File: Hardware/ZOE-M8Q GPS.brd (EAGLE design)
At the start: 25.4 x 25.4 mm, 23 parts, among them J4 U.FL, U1 UBLOX_ZOE_M8-0-10, Y1 32.768kHz

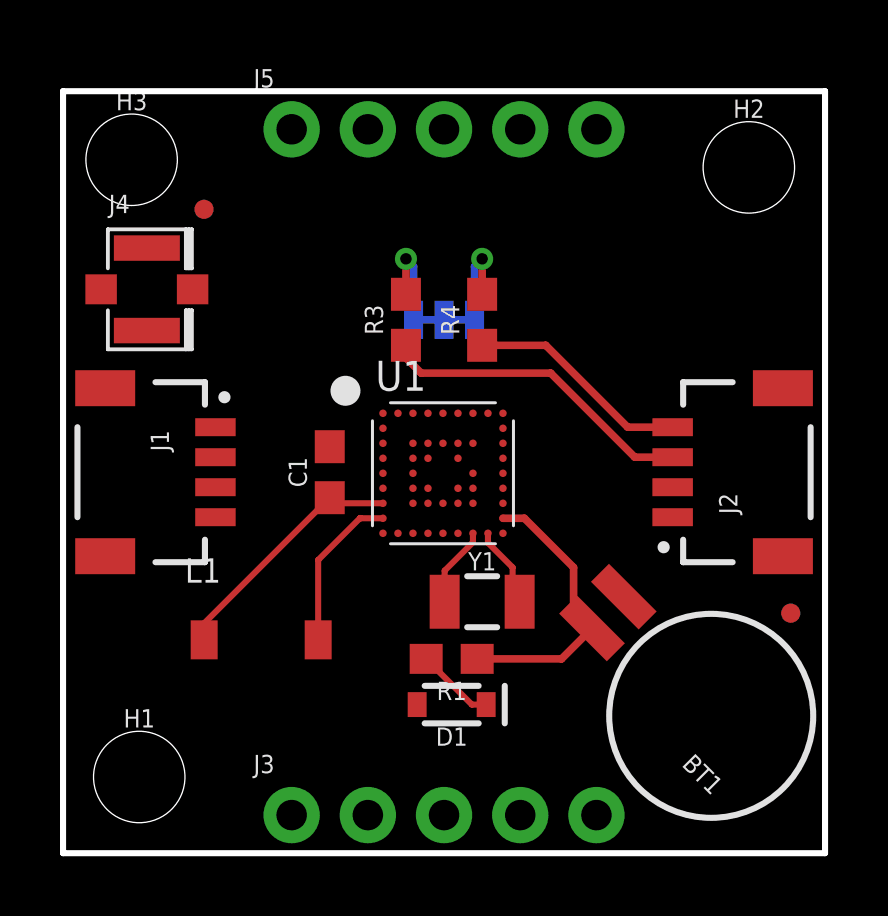
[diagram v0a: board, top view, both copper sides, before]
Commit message: Adds Buzzard Labels, finishes tracework (see description)
* Moves diode and reistor
* Fixes TSTOP on LGA
* Moves uFL connector
* Moves Jumpers
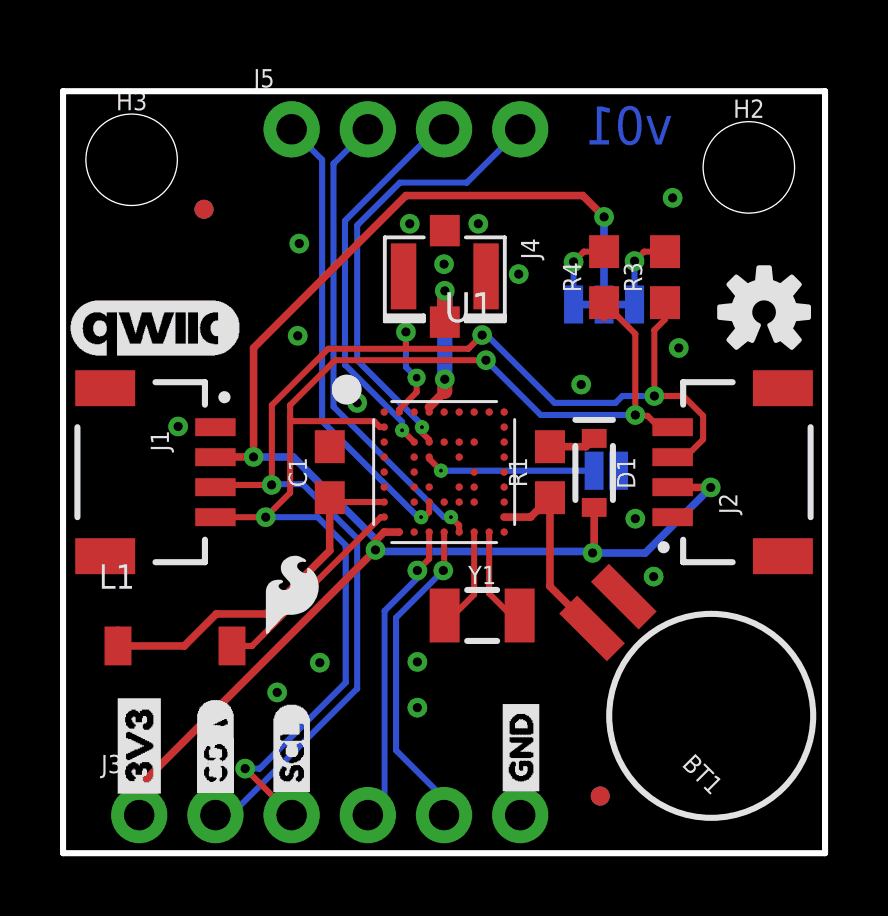
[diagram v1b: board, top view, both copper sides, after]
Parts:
- removed H1: STAND-OFFTIGHT, SparkFun-Hardware:STAND-OFF-TIGHT
- added JP1: JUMPER-SMT_2_NO_SILK, SparkFun-Jumpers:SMT-JUMPER_2_NO_SILK
- added LOGO1: SFE_LOGO_NAME.1_INCH, SparkFun-Aesthetics:SFE_LOGO_NAME_.1
- added LOGO2: OSHW-LOGOS, SparkFun-Aesthetics:OSHW-LOGO-S
- added LOGO3: SFE_LOGO_FLAME.1_INCH, SparkFun-Aesthetics:SFE_LOGO_FLAME_.1
- added U$1, U$10: (no value), Labels:3V3-03
- added U$11: (no value), INT:INT0
- added U$12: (no value), RESET:RESET0
- added U$13: (no value), TIMEPULSE:TIMEPULSE0
- added U$14: (no value), SAFEBOOT:SAFEBOOT0
- added U$15, U$19: (no value), Labels:QWIIC_COPYRIGHT_SMALL
- added U$16: (no value), ZOE-M8Q:ZOE#M8Q0
- added U$17: (no value), SPI_JUMPER:SPI0
- added U$18: (no value), I2C_PU:I2C_PU0
- added U$2: (no value), SDA:SDA0
- added U$3: (no value), SCL:SCL0
- added U$4, U$7: (no value), GND:GND0
- added U$5: (no value), RX_MOSI:RXI#MOSI0
- added U$6: (no value), TXO_MISO:TXO#MISO0
- added U$8: (no value), CLK:CLK0
- added U$9: (no value), CS:CS0
- J3: device SparkFun-Connectors:1X05_NO_SILK -> SparkFun-Connectors:1X06_NO_SILK
- J5: device SparkFun-Connectors:1X05_NO_SILK -> SparkFun-Connectors:1X04_NO_SILK
- moved J4 9.94 mm to (12.7, 19.2), turned to 270 degrees
- moved D1 9.07 mm to (17.7, 12.7), turned to 270 degrees
- moved FD2 8.80 mm to (17.9, 1.91)
- moved FD4 8.80 mm to (17.9, 1.91)
- moved R3 8.75 mm to (20.1, 19.2)
- moved R1 7.03 mm to (16.2, 12.7), turned to 90 degrees
- moved JP2 5.36 mm to (18.0, 18.3)
- moved J3 5.08 mm to (2.54, 1.27)
- moved R4 4.31 mm to (18.0, 19.2)
- moved U1 3.23 mm to (12.7, 12.7)
- moved L1 2.88 mm to (3.73, 6.91)
- moved Y1 0.46 mm to (14.0, 7.92)
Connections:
- removed net LNA_EN: U1.35
- removed net N$16: U1.36
- removed net N$4: JP2.1, R4.2
- removed net N$9: U1.50
- removed net RXD/MOSI: U1.22
- removed net TXD/MISO: U1.21
- new net N$1: JP2.1, R3.2
- new net RXI/MOSI: J3.4, U1.22
- new net TXO/MISO: J3.5, U1.21
- net 3.3V: now also J3.1
- net D_SEL: now also JP1.1
- net GND: now also J3.6, JP1.2
- net INT: now also J5.1
- net N$3: now also R4.2; no longer R3.2
- net RESET: now also J5.2
- net SAFEBOOT: now also J5.4
- net SCL/CLK: now also J3.3
- net SDA/CS: now also J3.2
- net TIMEPULSE: now also J5.3
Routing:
- net 3.3V: track 0.00 -> 55.7 mm, vias 0 -> 5
- net SCL/CLK: track 7.48 -> 42.5 mm, vias 0 -> 4
- net SDA/CS: track 10.7 -> 45.3 mm, vias 0 -> 5
- net RESET: track 0.00 -> 15.8 mm, vias 0 -> 1
- net INT: track 0.00 -> 15.4 mm, vias 0 -> 1
- net SAFEBOOT: track 0.00 -> 15.0 mm, vias 0 -> 1
- net TIMEPULSE: track 0.00 -> 12.9 mm, vias 0 -> 1
- net TXO/MISO: track 0.00 -> 10.8 mm, vias 0 -> 1
- net RXI/MOSI: track 0.00 -> 10.3 mm, vias 0 -> 1
- net D_SEL: track 0.00 -> 5.72 mm, vias 0 -> 1
- net N$5: track 0.00 -> 5.30 mm, vias 0 -> 2
- net N$6: track 8.32 -> 12.7 mm
- net N$4: track 3.32 -> 0.00 mm, vias 1 -> 0
- net V_BATT: track 9.57 -> 6.73 mm
- net N$1: track 0.00 -> 2.59 mm, vias 0 -> 1
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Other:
- board text added: "v01"

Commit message: Updates silk, adds new inductor, adds LED
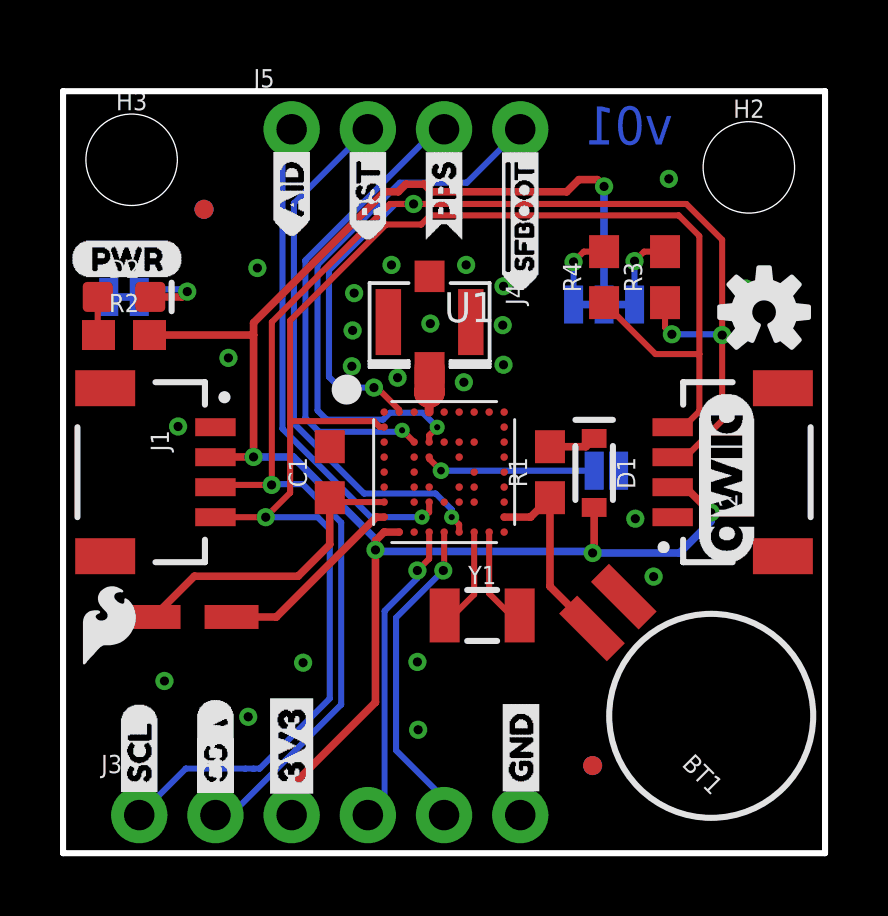
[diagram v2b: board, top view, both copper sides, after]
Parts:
- removed L1: 2.2µH/±20%/1.5A, SparkFun-Coils:INDUCTOR_2.2UH
- added D2: RED, SparkFun-LED:LED-0603
- added JP4: JUMPER-SMT_2_NC_TRACE_SILK, SparkFun-Jumpers:SMT-JUMPER_2_NC_TRACE_SILK
- added R2: 1k, SparkFun-Resistors:0603
- added U$20: 2.2UH_SHIELDED_INDUCTOR, temp:0806
- added U$21: (no value), AID:AID0
- added U$22: (no value), RESET:RST0
- added U$23: (no value), TIMEPULSE:PPS0
- added U$24: (no value), SAFEBOOT:#SFBOOT0
- added U$25: (no value), LED:LED0
- added U$26: (no value), Labels:PWR-()-03
- U$11: device INT:INT0 -> AID:AID0
- U$12: device RESET:RESET0 -> RESET:RST0
- U$13: device TIMEPULSE:TIMEPULSE0 -> TIMEPULSE:PPS0
- U$14: device SAFEBOOT:SAFEBOOT0 -> SAFEBOOT:#SFBOOT0
- moved U$15 19.7 mm to (22.1, 12.5), turned to 90 degrees
- moved LOGO3 6.18 mm to (1.52, 7.62)
- moved U$1 5.08 mm to (7.62, 1.52)
- moved U$10 5.08 mm to (7.62, 1.52)
- moved U$3 5.08 mm to (2.54, 1.68)
- moved U$8 5.08 mm to (2.54, 1.68)
- moved U$13 4.11 mm to (12.7, 20.4)
- moved U$14 2.11 mm to (15.2, 18.6), flipped to the top
- moved J4 1.61 mm to (12.2, 17.7)
- moved U$12 1.45 mm to (10.2, 20.4)
- moved FD2 1.05 mm to (17.7, 2.92)
- moved FD4 1.05 mm to (17.7, 2.92)
- moved U$11 0.05 mm to (7.62, 20.5)
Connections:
- new net N$4: D2.A, R2.1
- new net N$8: D2.C, JP4.2
- net 3.3V: now also J3.3, R2.2; no longer J3.1
- net GND: now also JP4.1
- net N$6: now also U$20.P$1; no longer L1.P$1
- net N$7: now also U$20.P$2; no longer L1.P$2
- net SCL/CLK: now also J3.1; no longer J3.3
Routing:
- net SDA/CS: track 45.3 -> 60.3 mm
- net SCL/CLK: track 42.5 -> 53.9 mm, vias 4 -> 1
- net N$5: track 5.30 -> 1.48 mm, vias 2 -> 0
- net SAFEBOOT: track 15.0 -> 18.5 mm
- net 3.3V: track 55.7 -> 59.0 mm
- net N$8: track 0.00 -> 3.04 mm, vias 0 -> 1
- net TIMEPULSE: track 12.9 -> 15.7 mm
- net RESET: track 15.8 -> 18.1 mm
- net N$6: track 12.7 -> 10.3 mm
- net N$4: track 0.00 -> 1.28 mm
- net INT: track 15.4 -> 16.6 mm
- net N$15: track 3.88 -> 3.35 mm

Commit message: Adds pinout for FTDI connection, updates NDUC and ZOE footprints with tkeepout and tdocu, fixes silk labels
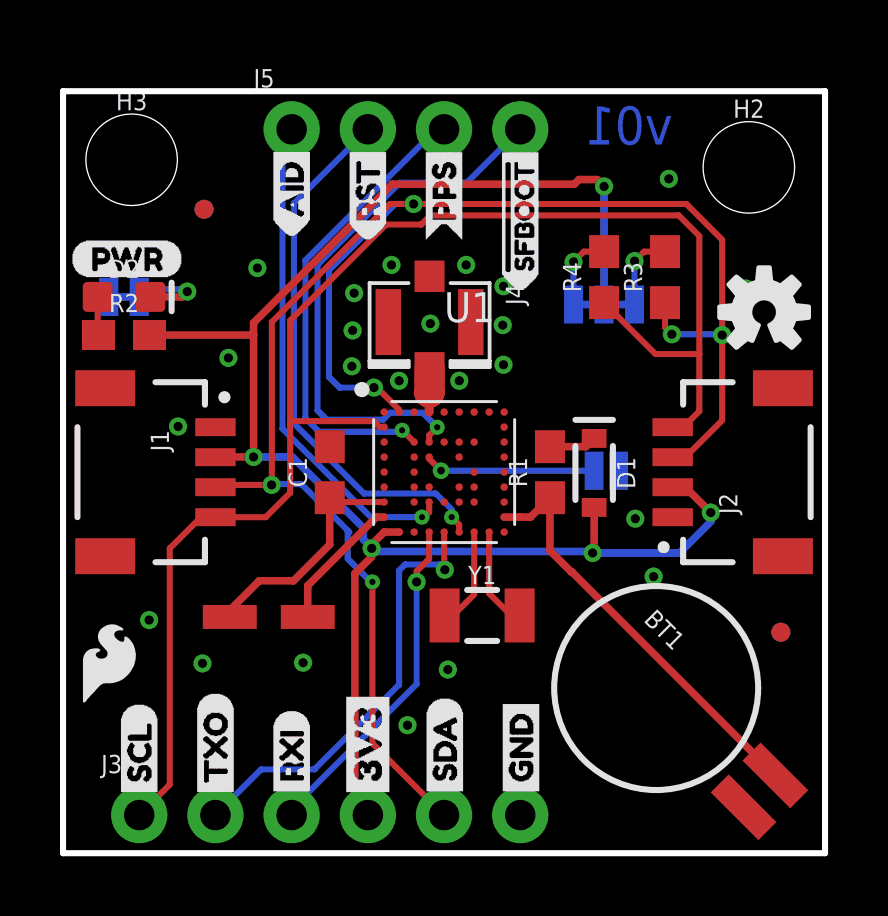
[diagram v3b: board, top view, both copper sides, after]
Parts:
- removed U$9: (no value), CS:CS0
- added U$27: (no value), MOSI:MOSI0
- U$15: device Labels:QWIIC_COPYRIGHT_SMALL -> TX:TXO0
- U$19: device Labels:QWIIC_COPYRIGHT_SMALL -> RX:RXI0
- U$20: device temp:0806 -> temp:0806_NDUC
- U$5: device RX_MOSI:RXI#MOSI0 -> CS:CS0
- U$6: device TXO_MISO:TXO#MISO0 -> MISO:MISO0
- moved U$15 20.2 mm to (5.08, 1.65)
- moved U$19 16.1 mm to (7.62, 1.70), flipped to the top, turned to 90 degrees
- moved FD2 7.69 mm to (23.9, 7.37)
- moved FD4 7.69 mm to (23.9, 7.37)
- moved U$2 7.65 mm to (12.7, 1.70)
- moved U$6 7.62 mm to (5.08, 1.65)
- moved U$5 2.57 mm to (12.7, 1.68)
- moved U$1 2.54 mm to (10.2, 1.57)
- moved U$10 2.54 mm to (10.2, 1.57)
- moved U$20 2.54 mm to (6.86, 7.87)
- moved BT1 2.06 mm to (19.8, 5.51), turned to 315 degrees
- moved LOGO3 1.27 mm to (1.52, 6.35)
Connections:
- net 3.3V: now also J3.4; no longer J3.3
- net RXI/MOSI: now also J3.3; no longer J3.4
- net SDA/CS: now also J3.5; no longer J3.2
- net TXO/MISO: now also J3.2; no longer J3.5
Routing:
- net V_BATT: track 6.73 -> 14.2 mm
- net SCL/CLK: track 53.9 -> 49.3 mm, vias 1 -> 0
- net TXO/MISO: track 10.8 -> 14.7 mm
- net N$6: track 10.3 -> 7.93 mm
- net N$7: track 6.47 -> 4.54 mm
- net RXI/MOSI: track 10.3 -> 11.3 mm
- net 3.3V: track 59.0 -> 58.1 mm
- net SDA/CS: track 60.3 -> 59.8 mm, vias 5 -> 6

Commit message: Adds more silk labels, adds tkeepout around oscillator and more ground vias
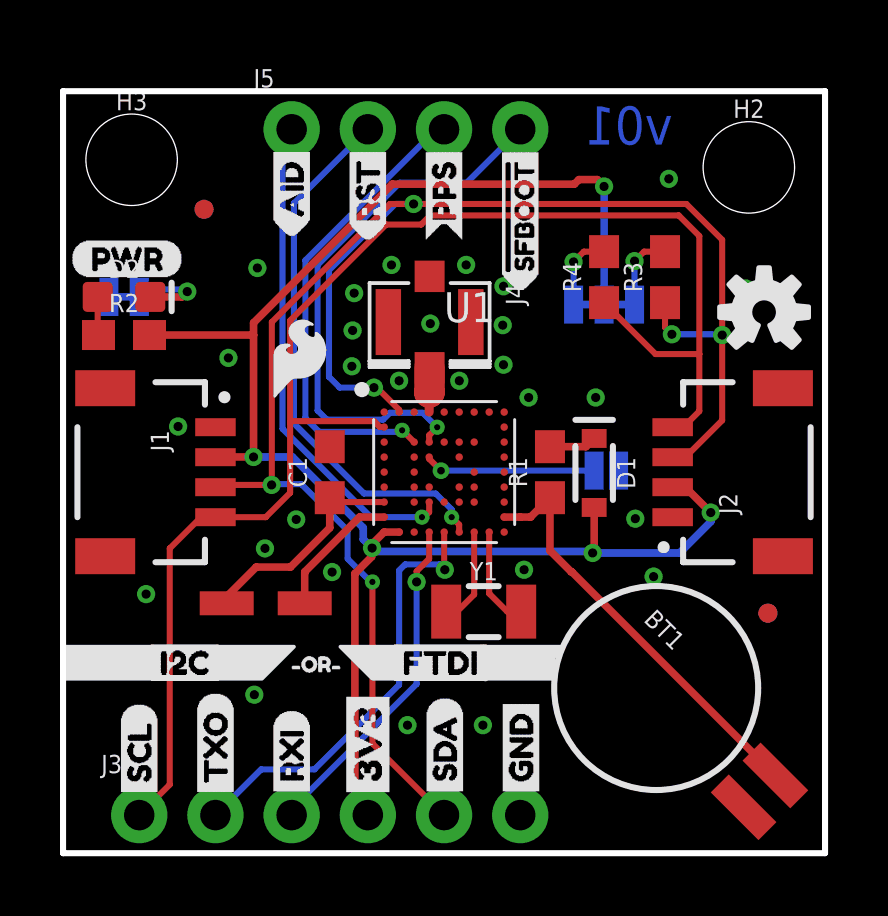
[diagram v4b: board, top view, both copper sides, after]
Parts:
- added U$28: (no value), I2C_MINOR:I2C0
- added U$29: (no value), FTDI_SMALL:FTDI0
- added U$30: (no value), OR:#OR#0
- added U$9: (no value), SPI_MAJOR:SPI0
- moved LOGO3 12.0 mm to (7.87, 16.5)
- moved FD2 0.77 mm to (23.5, 8.00)
- moved FD4 0.77 mm to (23.5, 8.00)
- moved U$20 0.47 mm to (6.76, 8.33)
- moved Y1 0.14 mm to (14.0, 8.05)
- moved U$18 0.13 mm to (20.4, 16.5)
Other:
- board text added: "Units in Inches"

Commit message: Removes one qwiic connector to make space for super capacitor, adds active antenna components (see description)
* Adds 10 ohm resistor, ferrite bead, and 47pF capacitor.
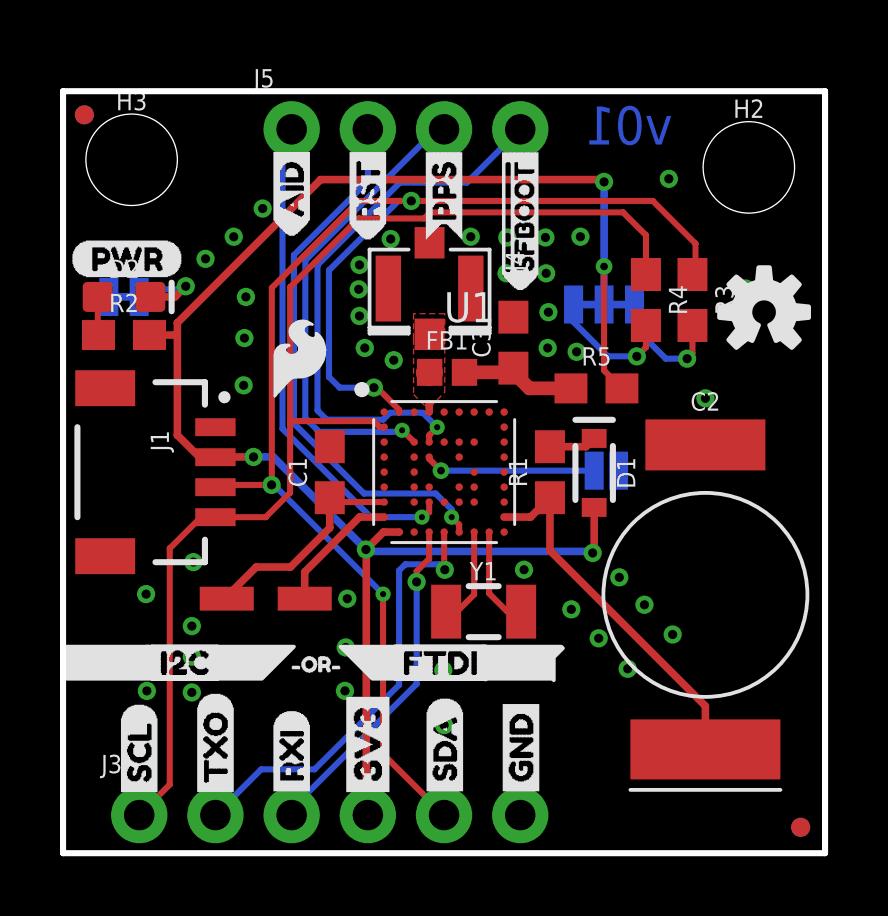
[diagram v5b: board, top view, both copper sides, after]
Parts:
- removed BT1: 6.8MM_COIN_CELL, SparkFun-Batteries:BATTCON-6.8MM
- removed J2: (no value), SparkFun-Connectors:JST04_1MM_RA
- removed U$20: 2.2UH_SHIELDED_INDUCTOR, temp:0806_NDUC
- added C2: .22F-SUPERCAP, SparkFun-Capacitors:DSK-RADIAL-4.8MM
- added C3: 47pF, SparkFun-Capacitors:0603
- added FB1: FERRITE_BEAD-120_OHM-0402, SparkFun-Coils:0402
- added L1: 2.2UH_SHIELDED_INDUCTOR, temp:0806_NDUC
- added R5: 10, SparkFun-Resistors:0603
- LOGO1: value SFE_LOGO_NAME.1_INCH -> SFE_LOGO_NAME_FLAME.1_INCH; device SparkFun-Aesthetics:SFE_LOGO_NAME_.1 -> SparkFun-Aesthetics:SFE_LOGO_NAME_FLAME_.1
- moved FD2 7.22 mm to (24.6, 0.86)
- moved FD4 7.22 mm to (24.6, 0.86)
- moved FD1 5.08 mm to (0.71, 24.6)
- moved FD3 5.08 mm to (0.71, 24.6)
- moved LOGO1 3.81 mm to (9.65, 15.0)
- moved R4 1.59 mm to (19.4, 18.4), turned to 270 degrees
- moved R3 1.19 mm to (21.0, 18.4), turned to 270 degrees
- moved J4 1.12 mm to (12.2, 18.8)
- moved U$16 0.53 mm to (12.8, 12.6)
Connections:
- removed net N$5: J4.FEED, U1.4
- new net ANT: FB1.1, J4.FEED, U1.4
- new net N$9: C3.1, FB1.2, R5.1
- net 3.3V: now also R5.2; no longer J2.2
- net GND: now also C2.-, C3.2; no longer BT1.-, J2.1
- net N$6: now also L1.P$1; no longer U$20.P$1
- net N$7: now also L1.P$2; no longer U$20.P$2
- net SCL/CLK: no longer J2.4
- net SDA/CS: no longer J2.3
- net V_BATT: now also C2.+; no longer BT1.+
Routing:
- net SDA/CS: track 59.7 -> 49.0 mm, vias 6 -> 4
- net SCL/CLK: track 49.3 -> 38.7 mm
- net N$9: track 0.00 -> 3.91 mm
- net V_BATT: track 14.2 -> 12.3 mm
- net N$3: track 2.58 -> 4.32 mm
- net N$1: track 2.59 -> 4.27 mm
- net 3.3V: track 58.1 -> 56.5 mm
- net N$5: track 1.48 -> 0.00 mm
- added copper zone on layer 1, net ANT

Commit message: Adds more ground stitching vias
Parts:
- moved LOGO3 3.10 mm to (4.90, 17.4)
- moved LOGO2 0.82 mm to (23.4, 17.2)
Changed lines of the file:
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@@
 <text x="20.32" y="23.622" size="1.27" layer="16" font="vector" ratio="15" rot="MR0">v01</text>
 <polygon width="0.127" layer="21">
-<vertex x="5.1308" y="5.8166"/>
-<vertex x="6.6294" y="5.8166"/>
-<vertex x="7.6962" y="6.8834"/>
-<vertex x="5.1054" y="6.8834"/>
-<vertex x="5.1054" y="5.8166"/>
+<vertex x="5.1308" y="5.801359375"/>
+<vertex x="6.614159375" y="5.801359375"/>
+<vertex x="7.711440625" y="6.898640625"/>
+<vertex x="5.1181" y="6.898640625"/>
+<vertex x="5.1181" y="5.8166"/>
 <vertex x="5.1562" y="5.8166"/>
 <vertex x="5.1562" y="5.842"/>
@@
 </polygon>
 <polygon width="0.127" layer="21">
-<vertex x="11.303" y="5.8166"/>
-<vertex x="10.3124" y="5.8166"/>
-<vertex x="9.2456" y="6.8834"/>
-<vertex x="11.15229375" y="6.8834"/>
-</polygon>
-<polygon width="0.127" layer="21">
-<vertex x="3.0226" y="6.8834"/>
-<vertex x="0" y="6.8834"/>
-<vertex x="0" y="5.8166"/>
-<vertex x="3.0734" y="5.8166"/>
+<vertex x="11.300459375" y="5.8013625"/>
+<vertex x="10.3276375" y="5.8013625"/>
+<vertex x="9.2329" y="6.8961"/>
+<vertex x="11.162453125" y="6.8961"/>
+</polygon>
+<polygon width="0.127" layer="21">
+<vertex x="3.0226" y="6.8961"/>
+<vertex x="0" y="6.8961"/>
+<vertex x="0" y="5.801359375"/>
+<vertex x="3.088640625" y="5.801359375"/>
 <vertex x="3.0226" y="5.8674"/>
 </polygon>
@@
 </polygon>
 <polygon width="0.127" layer="21">
-<vertex x="14.1732" y="5.8166"/>
-<vertex x="16.3068" y="5.8166"/>
-<vertex x="16.3576" y="5.7658"/>
-<vertex x="16.3576" y="6.5278"/>
-<vertex x="16.6624" y="6.8326"/>
-<vertex x="16.6116" y="6.8834"/>
-<vertex x="13.9192" y="6.8834"/>
-<vertex x="13.9192" y="5.9436"/>
-<vertex x="14.0716" y="5.7912"/>
-<vertex x="14.1732" y="5.8166"/>
+<vertex x="14.048459375" y="5.801359375"/>
+<vertex x="16.3449" y="5.801359375"/>
+<vertex x="16.3449" y="6.8707"/>
+<vertex x="16.3195" y="6.8961"/>
+<vertex x="13.9192" y="6.8961"/>
+<vertex x="13.9192" y="5.93061875"/>
 </polygon>
 <dimension x1="25.4" y1="25.4" x2="25.4" y2="0" x3="31.75" y3="12.7" textsize="1.27" textratio="15" layer="47" dtype="vertical" unit="inch"/>
@@
 <element name="U$10" library="Labels" package="3V3-03" value="" x="10.16" y="1.5748" smashed="yes" rot="MR90"/>
 <element name="LOGO1" library="SparkFun-Aesthetics" package="SFE_LOGO_NAME_FLAME_.1" value="SFE_LOGO_NAME_FLAME.1_INCH" x="9.652" y="14.986" smashed="yes" rot="MR0"/>
-<element name="LOGO2" library="SparkFun-Aesthetics" package="OSHW-LOGO-S" value="OSHW-LOGOS" x="23.368" y="18.034" smashed="yes"/>
+<element name="LOGO2" library="SparkFun-Aesthetics" package="OSHW-LOGO-S" value="OSHW-LOGOS" x="23.362921875" y="17.213578125" smashed="yes"/>
 <element name="U$16" library="ZOE-M8Q" package="ZOE#M8Q0" value="" x="12.7508" y="12.6238" smashed="yes" rot="MR0"/>
-<element name="LOGO3" library="SparkFun-Aesthetics" package="SFE_LOGO_FLAME_.1" value="SFE_LOGO_FLAME.1_INCH" x="7.874" y="16.51" smashed="yes"/>
+<element name="LOGO3" library="SparkFun-Aesthetics" package="SFE_LOGO_FLAME_.1" value="SFE_LOGO_FLAME.1_INCH" x="4.9047375" y="17.386303125" smashed="yes"/>
 <element name="U$17" library="SPI_JUMPER" package="SPI0" value="" x="19.558" y="10.922" smashed="yes" rot="MR0"/>
 <element name="U$18" library="I2C_PU" package="I2C_PU0" value="" x="20.447" y="16.51" smashed="yes" rot="MR0"/>
